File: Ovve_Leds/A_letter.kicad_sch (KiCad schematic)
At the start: 0 parts

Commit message: Finished preliminary schematics
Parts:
- added D1, D10, D11, D12, D2, D3, D4, D5, D6, D7, D8, D9: LED, symbol Device:LED
- added H10, H11, H12, H7, H8, H9: MountingHole, symbol Mechanical:MountingHole
- added R1, R10, R11, R12, R2, R3, R4, R5, R6, R7, R8, R9: 150, symbol Device:R
- added U1: 74LS174, symbol 74xx:74LS174
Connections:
- net CLK_in_A: now also U1.9 (Cp)
- net DATA_in_A: now also U1.3 (D0)
- net DATA_out_A: now also R11.1, R12.1, U1.12 (Q4)
- new net: D5.2 (A), R5.2
- new net: D1.2 (A), R1.2
- new net: D8.2 (A), R8.2
- new net: D3.2 (A), R3.2
- new net: D4.2 (A), R4.2
- new net: D10.2 (A), R10.2
- new net: D11.2 (A), R11.2
- new net: D7.2 (A), R7.2
- new net: D2.2 (A), R2.2
- new net: D6.2 (A), R6.2
- new net: D12.2 (A), R12.2
- new net: D9.2 (A), R9.2
- new net +5V: U1.1 (~{Mr}), U1.16 (VCC)
- new net GND: D1.1 (K), D10.1 (K), D11.1 (K), D12.1 (K), D2.1 (K), D3.1 (K), D4.1 (K), D5.1 (K), D6.1 (K), D7.1 (K), D8.1 (K), D9.1 (K), U1.8 (GND)
- new net LED1: R1.1, R2.1, R3.1, U1.2 (Q0), U1.4 (D1)
- new net LED2: R4.1, R5.1, U1.5 (Q1), U1.6 (D2)
- new net LED3: R6.1, R7.1, R8.1, U1.11 (D3), U1.7 (Q2)
- new net LED4: R10.1, R9.1, U1.10 (Q3), U1.13 (D4)
- no-connect marks 0 -> 2

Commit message: Added decoupling capacitors and assigned footprints
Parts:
- added C2: 0.1u, Capacitor_SMD:C_0603_1608Metric, symbol Device:C
- D1, D10, D11, D12, D2, D3, D4, D5, D6, D7, D8, D9: footprint (none) -> LED_THT:LED_D5.0mm
- H10, H11, H12, H7, H8, H9: footprint (none) -> MountingHole:MountingHole_5.3mm_M5_DIN965_Pad
- R1, R10, R11, R12, R2, R3, R4, R5, R6, R7, R8, R9: footprint (none) -> Resistor_SMD:R_0603_1608Metric
- U1: footprint (none) -> Package_DIP:DIP-16_W7.62mm
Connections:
- net +5V: now also C2.1
- net GND: now also C2.2

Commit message: Updated flip-flops
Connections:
- net GND: now also U1.14 (D5)
- no-connect marks 2 -> 1
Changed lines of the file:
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@@
-	)
-	(no_connect
-		(at 50.8 72.39)
 	)
 	(no_connect
@@
 	(wire
 		(pts
+			(xy 50.8 69.85) (xy 58.42 69.85)
+		)
+		(stroke
+			(width 0)
+			(type default)
+		)
+	)
+	(wire
+		(pts
+			(xy 78.74 29.21) (xy 78.74 34.29)
+		)
+		(stroke
+			(width 0)
+			(type default)
+		)
+	)
+	(wire
+		(pts
 			(xy 50.8 72.39) (xy 58.42 72.39)
-		)
-		(stroke
-			(width 0)
-			(type default)
-		)
-	)
-	(wire
-		(pts
-			(xy 50.8 69.85) (xy 58.42 69.85)
-		)
-		(stroke
-			(width 0)
-			(type default)
-		)
-	)
-	(wire
-		(pts
-			(xy 78.74 29.21) (xy 78.74 34.29)
 		)
 		(stroke
@@
 					(unit 1)
 				)
+			)
+		)
+	)
+	(symbol
+		(lib_id "power:GND")
+		(at 50.8 72.39 0)
+		(unit 1)
+		(exclude_from_sim no)
+		(in_bom yes)
+		(on_board yes)
+		(dnp no)
+		(property "Reference" "#PWR071"
+			(at 50.8 78.74 0)
+			(effects
+				(font
+					(size 1.27 1.27)
+				)
+				(hide yes)
+			)
+		)
+		(property "Value" "GND"
+			(at 50.8 76.2 0)
+			(effects
+				(font
+					(size 1.27 1.27)
+				)
+			)
+		)
+		(property "Footprint" ""
+			(at 50.8 72.39 0)
+			(effects
+				(font
+					(size 1.27 1.27)
+				)
+				(hide yes)
+			)
+		)
+		(property "Datasheet" ""
+			(at 50.8 72.39 0)
+			(effects
+				(font
+					(size 1.27 1.27)
+				)
+				(hide yes)
+			)
+		)
+		(property "Description" "Power symbol creates a global label with name \"GND\" , ground"
+			(at 50.8 72.39 0)
+			(effects
+				(font
+					(size 1.27 1.27)
+				)
+				(hide yes)
+			)
+		)
+		(pin "1"
+		)
+		(instances
+			(project "Ovve_Leds"
+				(path "/a3f154e4-ded7-4c3a-b779-1e1dc74aad12/480d303f-d31c-4223-9bbd-f91de5818754"
+					(reference "#PWR071")
+					(unit 1)
+				)

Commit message: Component layout on PCB
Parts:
- removed H10, H9: MountingHole, MountingHole:MountingHole_5.3mm_M5_DIN965_Pad, symbol Mechanical:MountingHole
- renumbered H8 to H10, H11 to H13, H12 to H14, H7 to H9

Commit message: Started work on new design with only one letter
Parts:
- removed H10, H13, H14, H9: MountingHole, MountingHole:MountingHole_5.3mm_M5_DIN965_Pad, symbol Mechanical:MountingHole
- added D13, D14, D15: LED, LED_THT:LED_D5.0mm, symbol Device:LED
- added H5, H6, H7, H8: MountingHole, MountingHole:MountingHole_5.3mm_M5_DIN965_Pad, symbol Mechanical:MountingHole
- added R13, R14, R15: 150, Resistor_SMD:R_0603_1608Metric, symbol Device:R
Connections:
- net GND: now also D13.1 (K), D14.1 (K), D15.1 (K)
- net LED2: now also R6.1
- net LED3: now also R9.1; no longer R6.1
- net LED4: now also R11.1, R12.1; no longer R9.1
- net CLK_in_A renamed CLK_in
- net DATA_in_A renamed DATA_in
- removed net DATA_out_A: R11.1, R12.1, U1.12 (Q4)
- new net: D13.2 (A), R13.2
- new net: D14.2 (A), R14.2
- new net: D15.2 (A), R15.2
- new net DATA_out: R13.1, R14.1, R15.1, U1.12 (Q4)

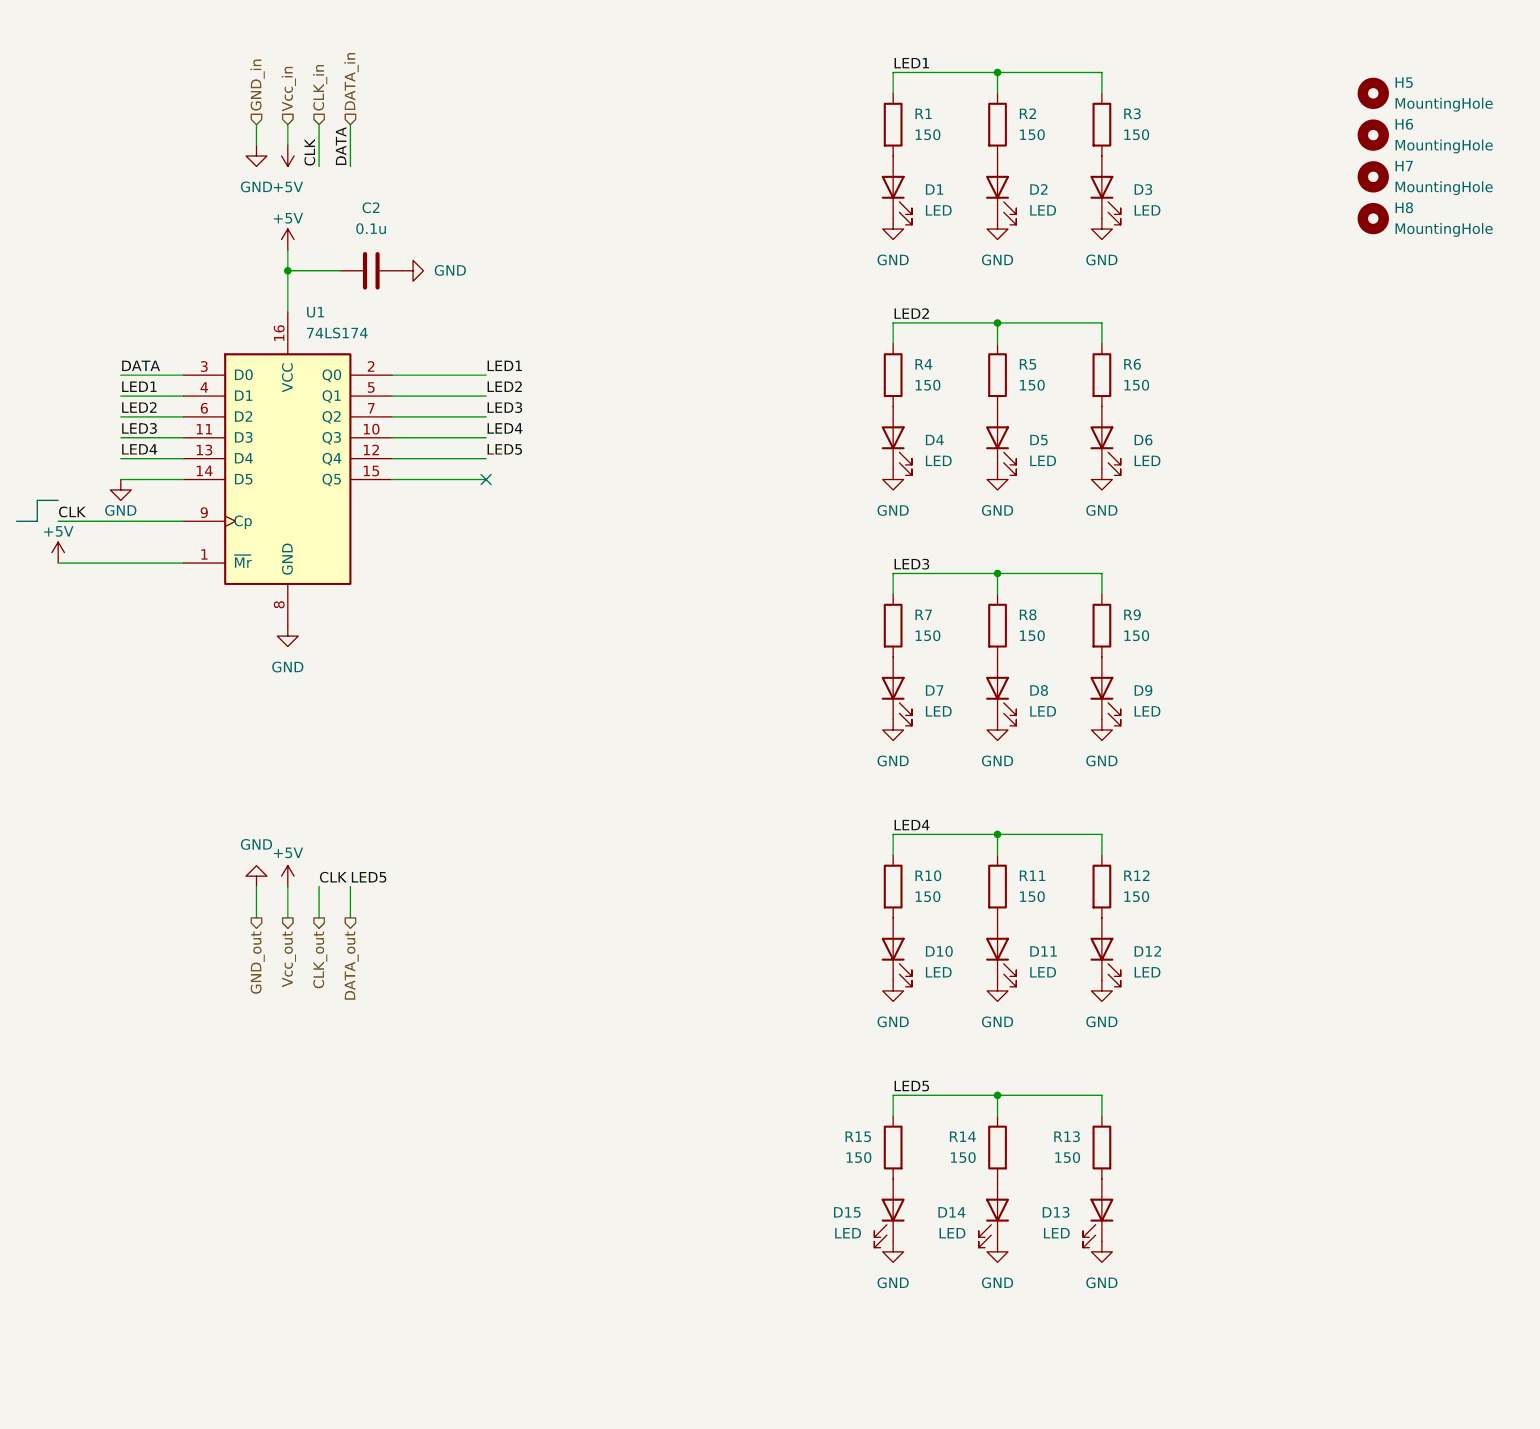
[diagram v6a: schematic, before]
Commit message: Added more LEDs to make letters more visible since there will be no silkscreen
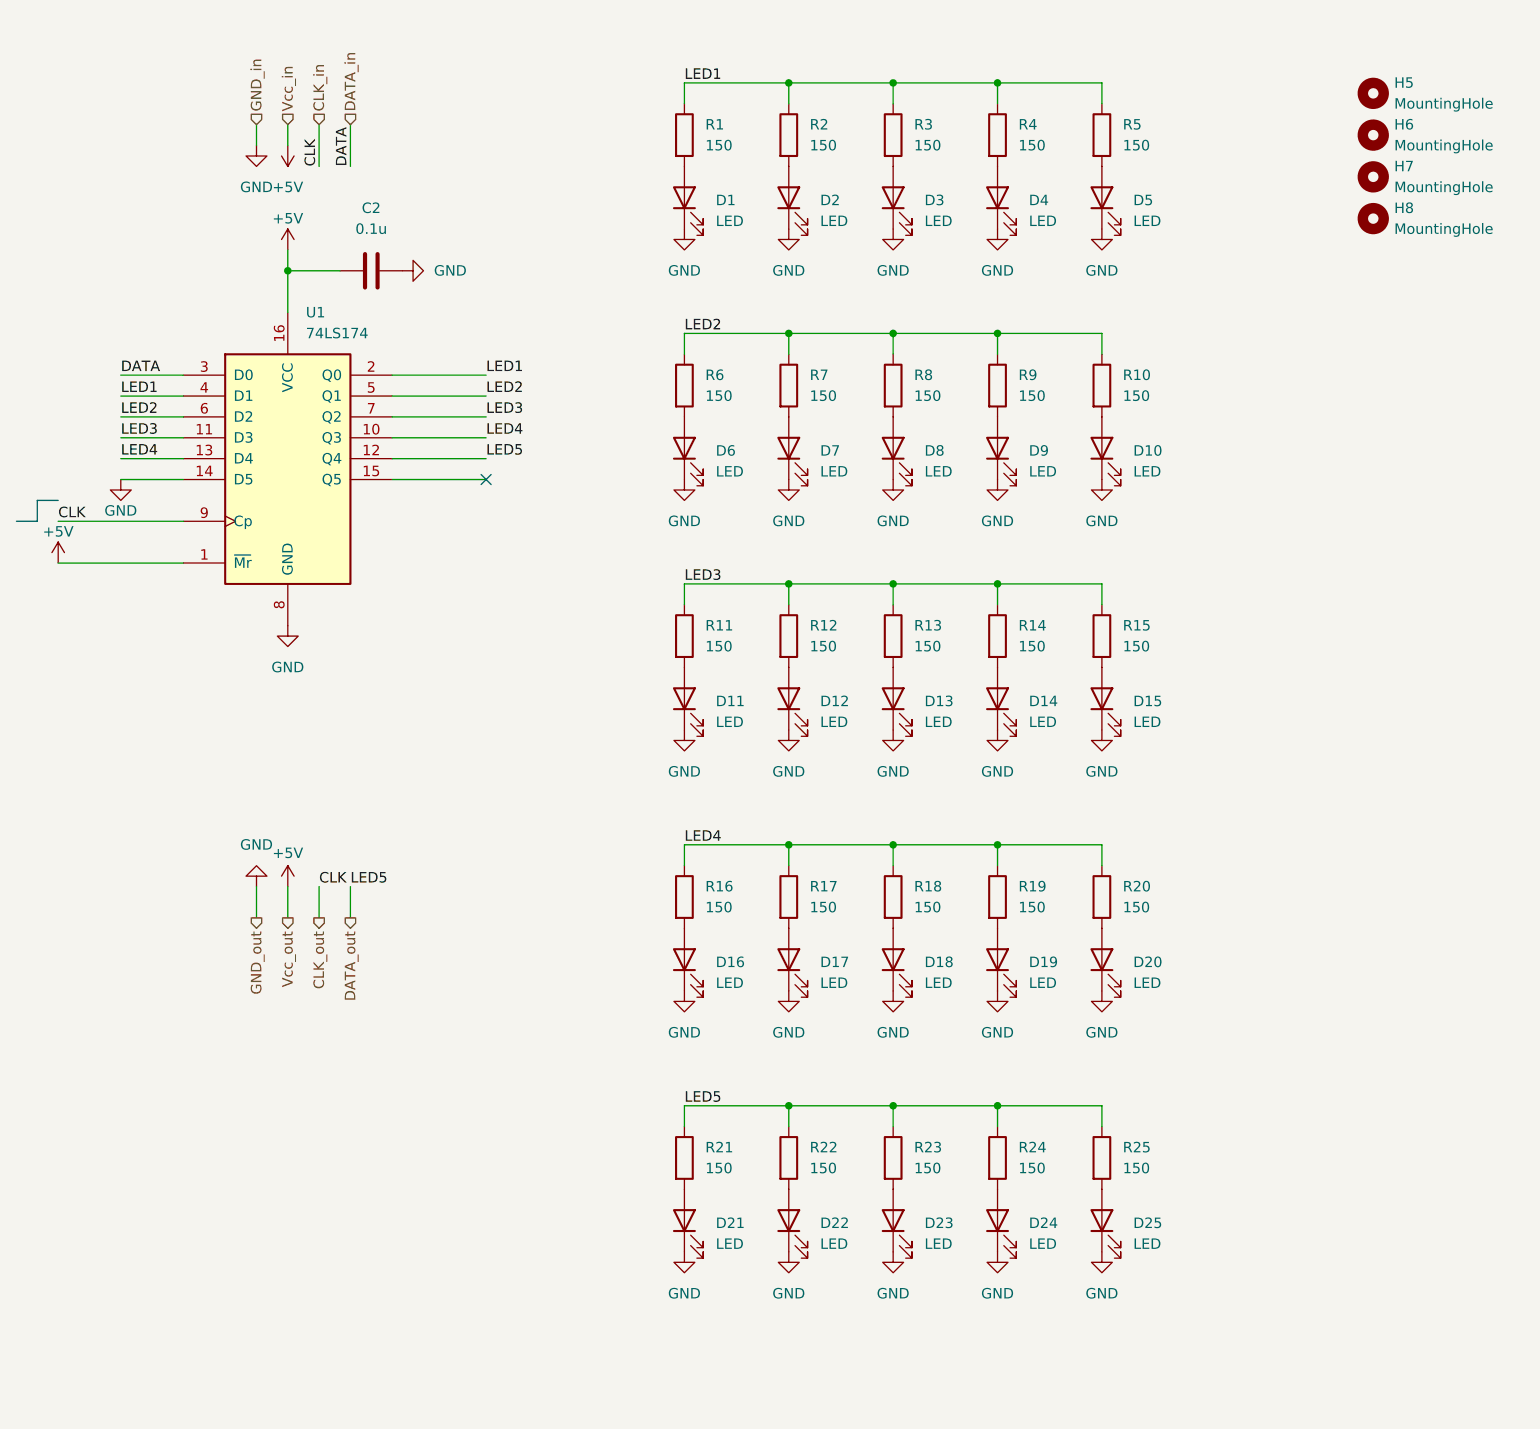
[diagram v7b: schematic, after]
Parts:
- added D16, D17, D18, D19, D20, D21, D22, D23, D24, D25: LED, LED_THT:LED_D5.0mm, symbol Device:LED
- added R16, R17, R18, R19, R20, R21, R22, R23, R24, R25: 150, Resistor_SMD:R_0603_1608Metric, symbol Device:R
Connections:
- net DATA_out: now also R21.1, R22.1, R23.1, R24.1, R25.1; no longer R13.1, R14.1, R15.1
- net GND: now also D16.1 (K), D17.1 (K), D18.1 (K), D19.1 (K), D20.1 (K), D21.1 (K), D22.1 (K), D23.1 (K), D24.1 (K), D25.1 (K)
- net LED1: now also R4.1, R5.1
- net LED2: now also R10.1, R7.1, R8.1, R9.1; no longer R4.1, R5.1
- net LED3: now also R11.1, R12.1, R13.1, R14.1, R15.1; no longer R7.1, R8.1, R9.1
- net LED4: now also R16.1, R17.1, R18.1, R19.1, R20.1; no longer R10.1, R11.1, R12.1
- new net: D19.2 (A), R19.2
- new net: D20.2 (A), R20.2
- new net: D17.2 (A), R17.2
- new net: D22.2 (A), R22.2
- new net: D24.2 (A), R24.2
- new net: D23.2 (A), R23.2
- new net: D18.2 (A), R18.2
- new net: D21.2 (A), R21.2
- new net: D16.2 (A), R16.2
- new net: D25.2 (A), R25.2

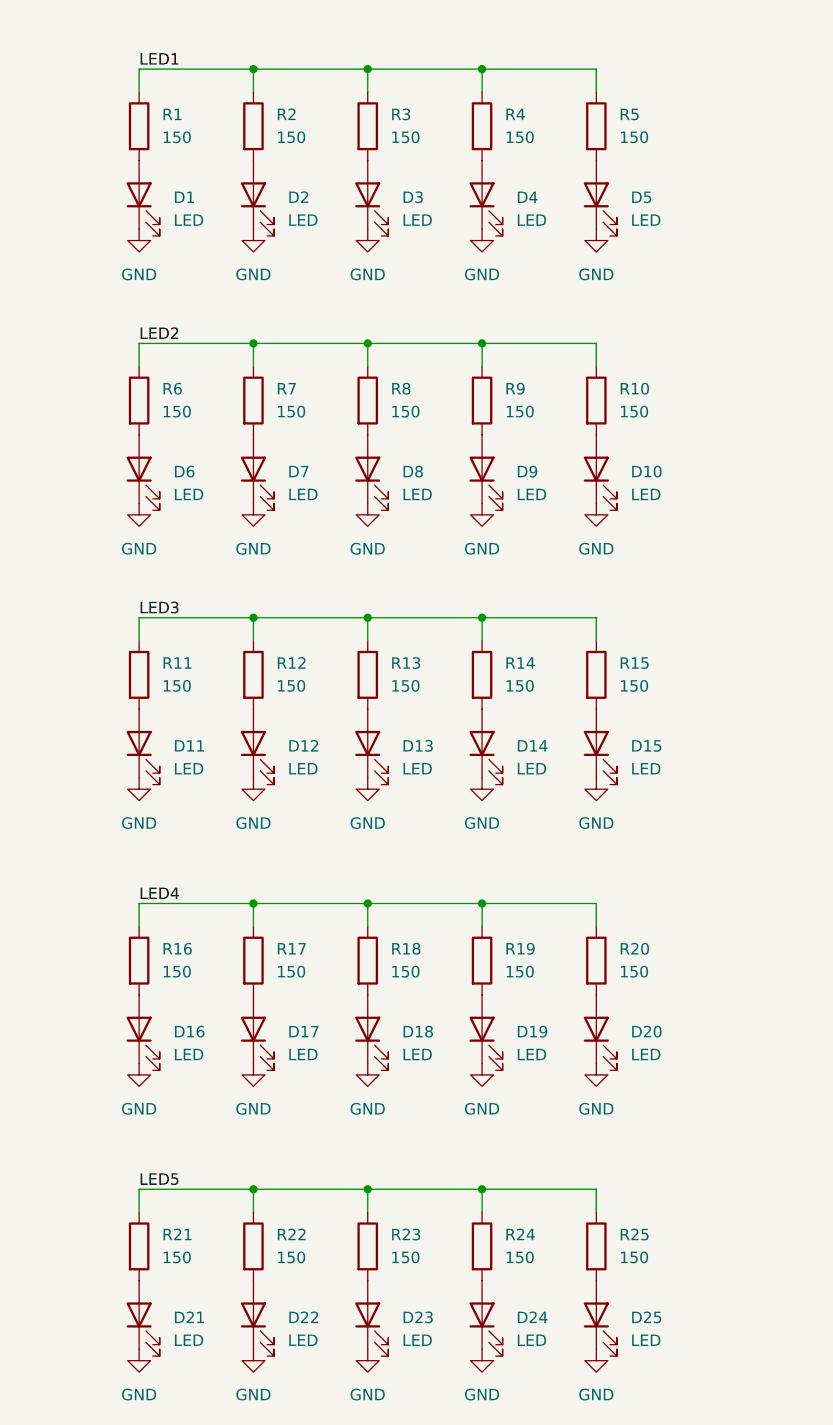
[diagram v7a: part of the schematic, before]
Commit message: Changed to 5x4
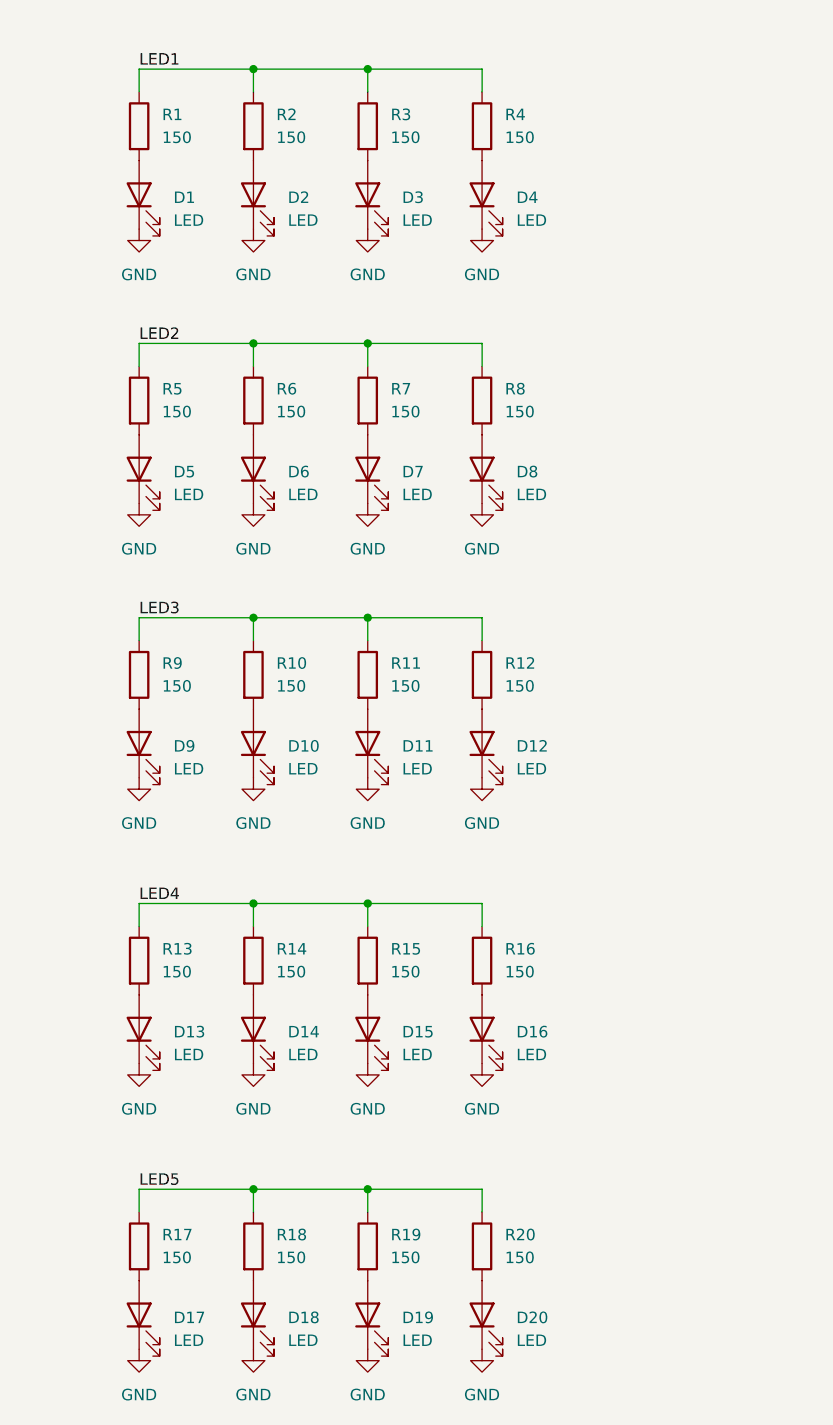
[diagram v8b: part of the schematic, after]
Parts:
- removed D21, D22, D23, D24, D25: LED, LED_THT:LED_D5.0mm, symbol Device:LED
- removed R21, R22, R23, R24, R25: 150, Resistor_SMD:R_0603_1608Metric, symbol Device:R
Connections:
- net DATA_out: now also R17.1, R18.1, R19.1, R20.1
- net LED1: no longer R5.1
- net LED2: now also R5.1; no longer R10.1, R9.1
- net LED3: now also R10.1, R9.1; no longer R13.1, R14.1, R15.1
- net LED4: now also R13.1, R14.1, R15.1; no longer R17.1, R18.1, R19.1, R20.1
